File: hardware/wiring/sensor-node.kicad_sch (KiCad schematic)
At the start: 7 parts, among them U1 ESP32-DevKitC, U2 BMP280, U3 DHT11, U4 LM35

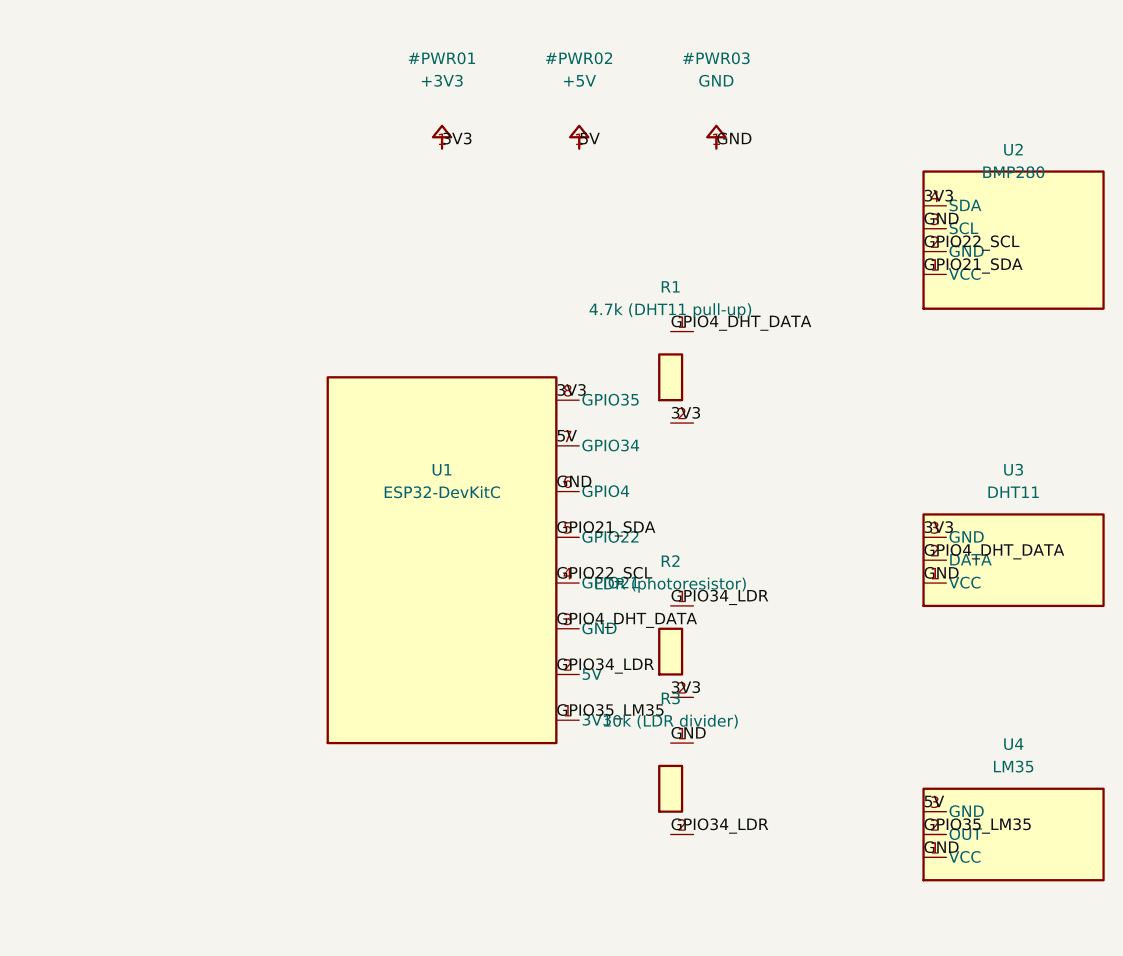
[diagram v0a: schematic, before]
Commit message: feat: change KiCad schema to be more readable + add schema ias png file
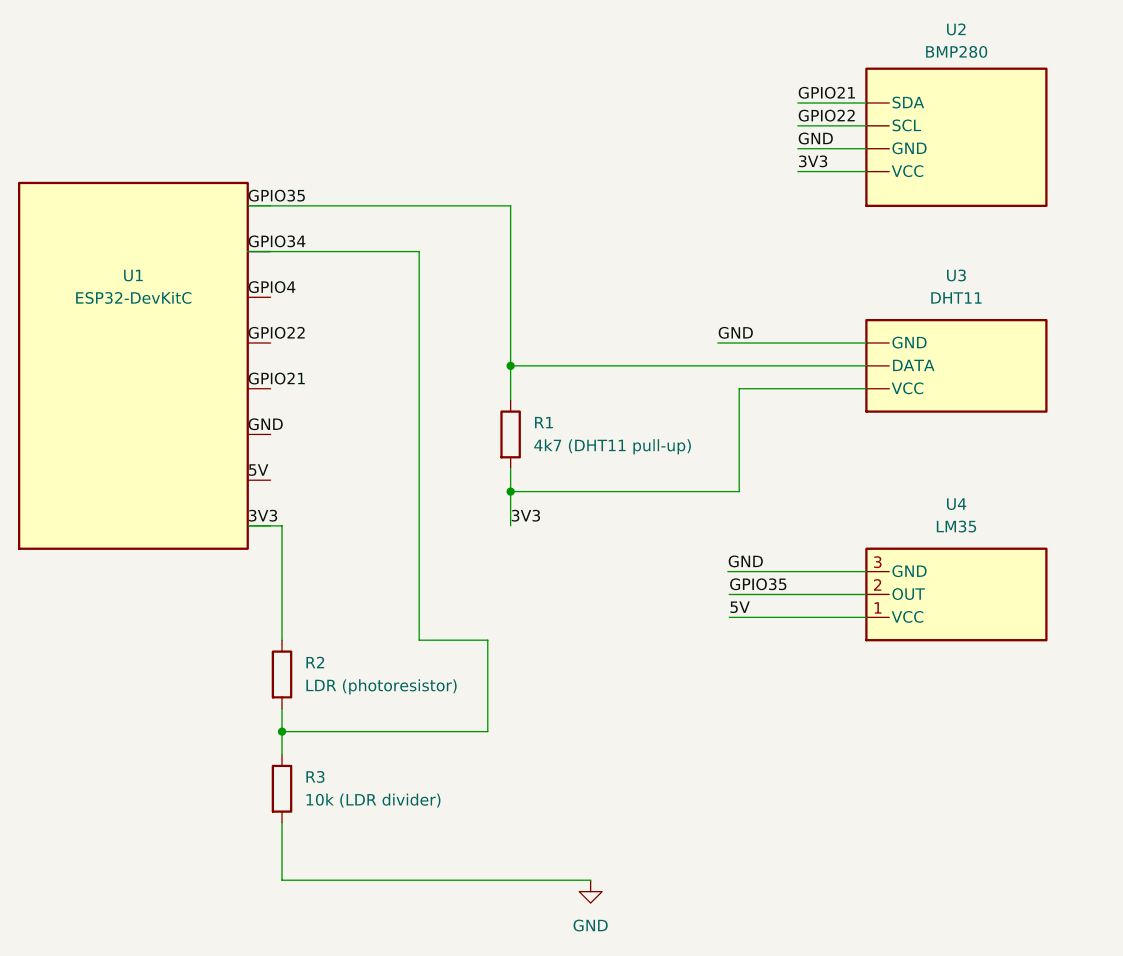
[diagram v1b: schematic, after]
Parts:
- removed R1: 4.7k (DHT11 pull-up), symbol Local:R
- removed R2: LDR (photoresistor), symbol Local:R
- removed R3: 10k (LDR divider), symbol Local:R
- added R1: 4k7 (DHT11 pull-up), symbol Device:R
- added R2: LDR (photoresistor), symbol Device:R
- added R3: 10k (LDR divider), symbol Device:R
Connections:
- net GND: now also U1.3 (GND), U2.2 (GND), U3.3 (GND), U4.3 (GND), R3.2; no longer U1.6 (GPIO4), U2.3 (SCL), U3.1 (VCC), U4.1 (VCC)
- removed net +3V3: U1.8 (GPIO35), U2.4 (SDA), U3.3 (GND)
- net +5V renamed GPIO34
- net GPIO34: now also R2.2, R3.1; no longer U4.3 (GND)
- net GPIO21_SDA renamed 3V3
- net 3V3: now also U1.1 (3V3), U3.1 (VCC), R1.2, R2.1; no longer U1.5 (GPIO22)
- net GPIO22_SCL renamed GPIO21
- net GPIO21: now also U2.4 (SDA); no longer U2.2 (GND)
- net GPIO34_LDR renamed 5V
- net 5V: now also U4.1 (VCC)
- net GPIO35_LM35 renamed GPIO35
- net GPIO35: now also U1.8 (GPIO35), U3.2 (DATA), R1.1; no longer U1.1 (3V3)
- removed net GPIO4_DHT_DATA: U1.3 (GND), U3.2 (DATA)
- new net GPIO22: U1.5 (GPIO22), U2.3 (SCL)
- new net GPIO4: U1.6 (GPIO4)
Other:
- company: secure-weather-station -> TESTSPECTIVE
- title: Sensor Node -- ESP32 #1 -- Combined Sensor Schematic -> secure-weather-station
- moved on the sheet: U4

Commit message: fix(hardware): fixing wrong waring DHT11 Data line
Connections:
- net GPIO35: no longer R1.1, U3.2 (DATA)
- net GPIO4: now also R1.1, U3.2 (DATA)
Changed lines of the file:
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@@
 	(title_block
 		(title "secure-weather-station")
-		(date "2026-09-05")
-		(rev "1.0")
+		(date "2026-09-07")
+		(rev "1.1")
 		(company "TESTSPECTIVE")
 		(comment 1 "Sensor Node")
@@
 	(wire
 		(pts
-			(xy 41.91 36.83) (xy 71.12 36.83)
-		)
-		(stroke
-			(width 0)
-			(type default)
-		)
-	)
-	(wire
-		(pts
 			(xy 68.58 85.09) (xy 60.96 85.09)
 		)
@@
 	(wire
 		(pts
+			(xy 71.12 46.99) (xy 71.12 54.61)
+		)
+		(stroke
+			(width 0)
+			(type default)
+		)
+	)
+	(wire
+		(pts
 			(xy 110.65 52.07) (xy 94.14 52.07)
 		)
@@
 	(wire
 		(pts
-			(xy 71.12 36.83) (xy 71.12 54.61)
-		)
-		(stroke
-			(width 0)
-			(type default)
-		)
-	)
-	(wire
-		(pts
 			(xy 110.65 33.02) (xy 103.03 33.02)
 		)
 		(stroke
+			(width 0)
+			(type default)
+		)
+	)
+	(wire
+		(pts
+			(xy 41.91 46.99) (xy 71.12 46.99)
+		)
+		(stroke
